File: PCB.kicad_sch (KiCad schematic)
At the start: 29 parts

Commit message: Rename and update layout
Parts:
- removed C1021, C1022, C1023, C1024, C1025, C1027, C1028: 100nF, Capacitor_SMD:C_0402_1005Metric, symbol Device:C
- removed H1002: MountingHole, SH-ESP32:MountingSlot_3.2mm_M3_Unplated, symbol Mechanical:MountingHole
- renumbered C1001 to C401, C1002 to C402, C1003 to C403, C1004 to C404, C1005 to C405, C1006 to C406, C1007 to C407, C1008 to C408, C1009 to C409, C1010 to C410, C1011 to C411, C1012 to C412, C1013 to C413, C1014 to C414, C1015 to C415, C1016 to C416, C1017 to C417, C1018 to C418, C1019 to C419, C1020 to C420, H1001 to H401
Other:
- title: Sailor Hat with ESP32 -> SH-wg

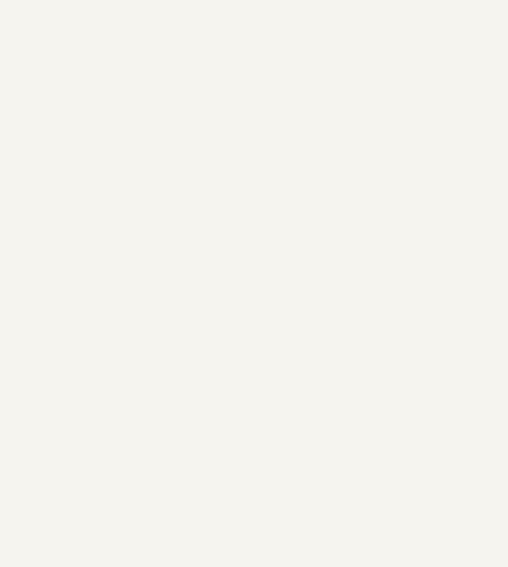
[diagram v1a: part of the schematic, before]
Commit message: Add headers & LEDs
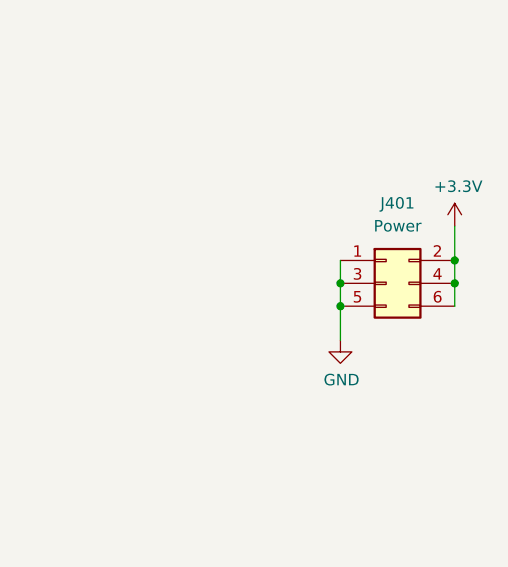
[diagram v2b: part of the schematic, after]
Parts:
- added J401: Power, Connector_PinHeader_2.54mm:PinHeader_2x03_P2.54mm_Vertical, symbol Connector_Generic:Conn_02x03_Odd_Even
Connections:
- net +3V3: now also J401.2 (Pin_2), J401.4 (Pin_4), J401.6 (Pin_6)
- net GND: now also J401.1 (Pin_1), J401.3 (Pin_3), J401.5 (Pin_5)
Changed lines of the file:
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@@
   (junction (at 99.06 62.23) (diameter 0) (color 0 0 0 0)
   )
+  (junction (at 162.56 62.23) (diameter 0) (color 0 0 0 0)
+  )
   (junction (at 91.44 52.07) (diameter 0) (color 0 0 0 0)
   )
@@
   (junction (at 91.44 118.11) (diameter 0) (color 0 0 0 0)
   )
+  (junction (at 162.56 59.69) (diameter 0) (color 0 0 0 0)
+  )
+  (junction (at 149.86 62.23) (diameter 0) (color 0 0 0 0)
+  )
   (junction (at 99.06 113.03) (diameter 0) (color 0 0 0 0)
   )
@@
   (junction (at 99.06 128.27) (diameter 0) (color 0 0 0 0)
   )
+  (junction (at 149.86 64.77) (diameter 0) (color 0 0 0 0)
+  )
   (junction (at 91.44 72.39) (diameter 0) (color 0 0 0 0)
   )
@@
     (stroke (width 0) (type default) (color 0 0 0 0))
   )
+  (wire (pts (xy 162.56 59.69) (xy 162.56 62.23))
+    (stroke (width 0) (type default) (color 0 0 0 0))
+  )
   (wire (pts (xy 99.06 118.11) (xy 99.06 113.03))
     (stroke (width 0) (type default) (color 0 0 0 0))
@@
     (stroke (width 0) (type default) (color 0 0 0 0))
   )
+  (wire (pts (xy 149.86 62.23) (xy 149.86 64.77))
+    (stroke (width 0) (type default) (color 0 0 0 0))
+  )
   (wire (pts (xy 99.06 97.79) (xy 99.06 92.71))
     (stroke (width 0) (type default) (color 0 0 0 0))
@@
     (stroke (width 0) (type default) (color 0 0 0 0))
   )
+  (wire (pts (xy 162.56 55.88) (xy 162.56 59.69))
+    (stroke (width 0) (type default) (color 0 0 0 0))
+  )
   (wire (pts (xy 91.44 57.15) (xy 91.44 62.23))
     (stroke (width 0) (type default) (color 0 0 0 0))
@@
     (stroke (width 0) (type default) (color 0 0 0 0))
   )
+  (wire (pts (xy 162.56 62.23) (xy 162.56 64.77))
+    (stroke (width 0) (type default) (color 0 0 0 0))
+  )
   (wire (pts (xy 91.44 92.71) (xy 91.44 97.79))
     (stroke (width 0) (type default) (color 0 0 0 0))
@@
     (stroke (width 0) (type default) (color 0 0 0 0))
   )
+  (wire (pts (xy 149.86 64.77) (xy 149.86 68.58))
+    (stroke (width 0) (type default) (color 0 0 0 0))
+  )
   (wire (pts (xy 99.06 57.15) (xy 99.06 52.07))
+    (stroke (width 0) (type default) (color 0 0 0 0))
+  )
+  (wire (pts (xy 149.86 59.69) (xy 149.86 62.23))
     (stroke (width 0) (type default) (color 0 0 0 0))
   )
@@
       (effects (font (size 1.27 1.27)) hide)
     )
+    (pin "1")
+  )
+  (symbol (lib_id "Connector_Generic:Conn_02x03_Odd_Even") (at 154.94 62.23 0) (unit 1)
+    (in_bom yes) (on_board yes) (fields_autoplaced)
+    (property "Reference" "J401" (id 0) (at 156.21 53.34 0))
+    (property "Value" "Power" (id 1) (at 156.21 55.88 0))
+    (property "Footprint" "Connector_PinHeader_2.54mm:PinHeader_2x03_P2.54mm_Vertical" (id 2) (at 154.94 62.23 0)
+      (effects (font (size 1.27 1.27)) hide)
+    )
+    (property "Datasheet" "~" (id 3) (at 154.94 62.23 0)
+      (effects (font (size 1.27 1.27)) hide)
+    )
+    (pin "1")
+    (pin "2")
+    (pin "3")
+    (pin "4")
+    (pin "5")
+    (pin "6")
+  )
+  (symbol (lib_id "power:+3.3V") (at 162.56 55.88 0) (unit 1)
+    (in_bom yes) (on_board yes)
+    (property "Reference" "#PWR0404" (id 0) (at 162.56 59.69 0)
+      (effects (font (size 1.27 1.27)) hide)
+    )
+    (property "Value" "+3.3V" (id 1) (at 162.941 51.4858 0))
+    (property "Footprint" "" (id 2) (at 162.56 55.88 0)
+      (effects (font (size 1.27 1.27)) hide)
+    )
+    (property "Datasheet" "" (id 3) (at 162.56 55.88 0)
+      (effects (font (size 1.27 1.27)) hide)
+    )
+    (pin "1")
+  )
+  (symbol (lib_id "power:GND") (at 149.86 68.58 0) (unit 1)
+    (in_bom yes) (on_board yes)
+    (property "Reference" "#PWR0403" (id 0) (at 149.86 74.93 0)
+      (effects (font (size 1.27 1.27)) hide)
+    )
+    (property "Value" "GND" (id 1) (at 149.987 72.9742 0))
+    (property "Footprint" "" (id 2) (at 149.86 68.58 0)
+      (effects (font (size 1.27 1.27)) hide)
+    )
+    (property "Datasheet" "" (id 3) (at 149.86 68.58 0)
+      (effects (font (size 1.27 1.27)) hide)
+    )

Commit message: Finish 0.1.0 design
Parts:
- removed C401, C402, C403, C404, C405, C407, C408, C409, C411, C412: 100nF, Capacitor_SMD:C_0402_1005Metric, symbol Device:C
- added G401: Hat Labs pictogram, SH-wg:HL_pictogram_6.3mm, symbol SH-wg:Image
- added G402: Hat Labs logo, SH-wg:Hat_Labs_20mm, symbol SH-wg:Image
- added G403: Hat Labs logo large, SH-wg:Hat_Labs_25.4mm, symbol SH-wg:Image
- added G404: WEEE logo, Symbol:WEEE-Logo_5.6x8mm_SilkScreen, symbol SH-wg:Image
- added G405: OSHW logo, Symbol:OSHW-Logo2_9.8x8mm_SilkScreen, symbol SH-wg:Image
- H401: footprint SH-ESP32:MountingSlot_3.2mm_M3_Unplated -> MountingHole:MountingHole_3.2mm_M3
- J401: LCSC (none) -> C65114
- renumbered C406 to C401, C410 to C402, C413 to C403, C414 to C404, C415 to C405, C416 to C406, C417 to C407, C418 to C408, C419 to C409, C420 to C410
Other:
- title: SH-wg -> Sailor Hat WiFi Gateway

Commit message: Prepare final 0.1.0 proto
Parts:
- H404: renamed from H401; now left out of the parts list
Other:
- moved on the sheet: G401, G402, G403, G404, G405
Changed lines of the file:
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@@
   )
   (symbol (lib_id "Mechanical:MountingHole") (at 48.26 46.99 0) (unit 1)
-    (in_bom yes) (on_board yes)
-    (property "Reference" "H401" (id 0) (at 50.8 45.8216 0)
+    (in_bom no) (on_board yes)
+    (property "Reference" "H404" (id 0) (at 50.8 45.8216 0)
       (effects (font (size 1.27 1.27)) (justify left))
     )
@@
     (pin "6")
   )
-  (symbol (lib_id "SH-wg:Image") (at 48.26 115.57 0) (unit 1)
-    (in_bom no) (on_board yes) (fields_autoplaced)
-    (property "Reference" "G404" (id 0) (at 52.07 114.2999 0)
-      (effects (font (size 1.27 1.27)) (justify left))
-    )
-    (property "Value" "WEEE logo" (id 1) (at 52.07 116.8399 0)
-      (effects (font (size 1.27 1.27)) (justify left))
-    )
-    (property "Footprint" "Symbol:WEEE-Logo_5.6x8mm_SilkScreen" (id 2) (at 48.26 115.57 0)
-      (effects (font (size 1.27 1.27)) hide)
-    )
-    (property "Datasheet" "" (id 3) (at 48.26 115.57 0)
-      (effects (font (size 1.27 1.27)) hide)
-    )
-  )
-  (symbol (lib_id "SH-wg:Image") (at 48.26 124.46 0) (unit 1)
-    (in_bom no) (on_board yes) (fields_autoplaced)
-    (property "Reference" "G405" (id 0) (at 52.07 123.1899 0)
-      (effects (font (size 1.27 1.27)) (justify left))
-    )
-    (property "Value" "OSHW logo" (id 1) (at 52.07 125.7299 0)
-      (effects (font (size 1.27 1.27)) (justify left))
-    )
-    (property "Footprint" "Symbol:OSHW-Logo2_9.8x8mm_SilkScreen" (id 2) (at 48.26 124.46 0)
-      (effects (font (size 1.27 1.27)) hide)
-    )
-    (property "Datasheet" "" (id 3) (at 48.26 124.46 0)
+  (symbol (lib_id "SH-wg:Image") (at 151.13 124.46 0) (unit 1)
+    (in_bom no) (on_board yes) (fields_autoplaced)
+    (property "Reference" "G404" (id 0) (at 154.94 123.1899 0)
+      (effects (font (size 1.27 1.27)) (justify left))
+    )
+    (property "Value" "WEEE logo" (id 1) (at 154.94 125.7299 0)
+      (effects (font (size 1.27 1.27)) (justify left))
+    )
+    (property "Footprint" "Symbol:WEEE-Logo_5.6x8mm_SilkScreen" (id 2) (at 151.13 124.46 0)
+      (effects (font (size 1.27 1.27)) hide)
+    )
+    (property "Datasheet" "" (id 3) (at 151.13 124.46 0)
+      (effects (font (size 1.27 1.27)) hide)
+    )
+  )
+  (symbol (lib_id "SH-wg:Image") (at 151.13 133.35 0) (unit 1)
+    (in_bom no) (on_board yes) (fields_autoplaced)
+    (property "Reference" "G405" (id 0) (at 154.94 132.0799 0)
+      (effects (font (size 1.27 1.27)) (justify left))
+    )
+    (property "Value" "OSHW logo" (id 1) (at 154.94 134.6199 0)
+      (effects (font (size 1.27 1.27)) (justify left))
+    )
+    (property "Footprint" "Symbol:OSHW-Logo2_9.8x8mm_SilkScreen" (id 2) (at 151.13 133.35 0)
+      (effects (font (size 1.27 1.27)) hide)
+    )
+    (property "Datasheet" "" (id 3) (at 151.13 133.35 0)
       (effects (font (size 1.27 1.27)) hide)
     )
@@
     (pin "1")
   )
-  (symbol (lib_id "SH-wg:Image") (at 48.26 97.79 0) (unit 1)
-    (in_bom no) (on_board yes) (fields_autoplaced)
-    (property "Reference" "G403" (id 0) (at 52.07 96.5199 0)
-      (effects (font (size 1.27 1.27)) (justify left))
-    )
-    (property "Value" "Hat Labs logo large" (id 1) (at 52.07 99.0599 0)
-      (effects (font (size 1.27 1.27)) (justify left))
-    )
-    (property "Footprint" "SH-wg:Hat_Labs_25.4mm" (id 2) (at 48.26 97.79 0)
-      (effects (font (size 1.27 1.27)) hide)
-    )
-    (property "Datasheet" "" (id 3) (at 48.26 97.79 0)
-      (effects (font (size 1.27 1.27)) hide)
-    )
-  )
-  (symbol (lib_id "SH-wg:Image") (at 48.26 88.9 0) (unit 1)
-    (in_bom no) (on_board yes) (fields_autoplaced)
-    (property "Reference" "G402" (id 0) (at 52.07 87.6299 0)
-      (effects (font (size 1.27 1.27)) (justify left))
-    )
-    (property "Value" "Hat Labs logo" (id 1) (at 52.07 90.1699 0)
-      (effects (font (size 1.27 1.27)) (justify left))
-    )
-    (property "Footprint" "SH-wg:Hat_Labs_20mm" (id 2) (at 48.26 88.9 0)
-      (effects (font (size 1.27 1.27)) hide)
-    )
-    (property "Datasheet" "" (id 3) (at 48.26 88.9 0)
+  (symbol (lib_id "SH-wg:Image") (at 151.13 106.68 0) (unit 1)
+    (in_bom no) (on_board yes) (fields_autoplaced)
+    (property "Reference" "G403" (id 0) (at 154.94 105.4099 0)
+      (effects (font (size 1.27 1.27)) (justify left))
+    )
+    (property "Value" "Hat Labs logo large" (id 1) (at 154.94 107.9499 0)
+      (effects (font (size 1.27 1.27)) (justify left))
+    )
+    (property "Footprint" "SH-wg:Hat_Labs_25.4mm" (id 2) (at 151.13 106.68 0)
+      (effects (font (size 1.27 1.27)) hide)
+    )
+    (property "Datasheet" "" (id 3) (at 151.13 106.68 0)
+      (effects (font (size 1.27 1.27)) hide)
+    )
+  )
+  (symbol (lib_id "SH-wg:Image") (at 151.13 97.79 0) (unit 1)
+    (in_bom no) (on_board yes) (fields_autoplaced)
+    (property "Reference" "G402" (id 0) (at 154.94 96.5199 0)
+      (effects (font (size 1.27 1.27)) (justify left))
+    )
+    (property "Value" "Hat Labs logo" (id 1) (at 154.94 99.0599 0)
+      (effects (font (size 1.27 1.27)) (justify left))
+    )
+    (property "Footprint" "SH-wg:Hat_Labs_20mm" (id 2) (at 151.13 97.79 0)
+      (effects (font (size 1.27 1.27)) hide)
+    )
+    (property "Datasheet" "" (id 3) (at 151.13 97.79 0)
       (effects (font (size 1.27 1.27)) hide)
     )
@@
     (pin "1")
   )
-  (symbol (lib_id "SH-wg:Image") (at 48.26 80.01 0) (unit 1)
-    (in_bom no) (on_board yes) (fields_autoplaced)
-    (property "Reference" "G401" (id 0) (at 52.07 78.7399 0)
-      (effects (font (size 1.27 1.27)) (justify left))
-    )
-    (property "Value" "Hat Labs pictogram" (id 1) (at 52.07 81.2799 0)
-      (effects (font (size 1.27 1.27)) (justify left))
-    )
-    (property "Footprint" "SH-wg:HL_pictogram_6.3mm" (id 2) (at 48.26 80.01 0)
-      (effects (font (size 1.27 1.27)) hide)
-    )
-    (property "Datasheet" "" (id 3) (at 48.26 80.01 0)
-      (effects (font (size 1.27 1.27)) hide)
-    )
+  (symbol (lib_id "SH-wg:Image") (at 151.13 88.9 0) (unit 1)
+    (in_bom no) (on_board yes) (fields_autoplaced)
+    (property "Reference" "G401" (id 0) (at 154.94 87.6299 0)
+      (effects (font (size 1.27 1.27)) (justify left))
+    )
+    (property "Value" "Hat Labs pictogram" (id 1) (at 154.94 90.1699 0)
+      (effects (font (size 1.27 1.27)) (justify left))
+    )
+    (property "Footprint" "SH-wg:HL_pictogram_6.3mm" (id 2) (at 151.13 88.9 0)
+      (effects (font (size 1.27 1.27)) hide)
+    )
+    (property "Datasheet" "" (id 3) (at 151.13 88.9 0)
+      (effects (font (size 1.27 1.27)) hide)
+    )

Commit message: Add copper clearance around the mounting hole
Also make the M12 connector opening 1.5mm wider.
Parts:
- H404: footprint MountingHole:MountingHole_3.2mm_M3 -> SH-wg:MountingHole_3.2mm_M3_no_copper
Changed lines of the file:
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@@
       (effects (font (size 1.27 1.27)) (justify left))
     )
-    (property "Footprint" "MountingHole:MountingHole_3.2mm_M3" (id 2) (at 48.26 46.99 0)
+    (property "Footprint" "SH-wg:MountingHole_3.2mm_M3_no_copper" (id 2) (at 48.26 46.99 0)
       (effects (font (size 1.27 1.27)) hide)
     )
